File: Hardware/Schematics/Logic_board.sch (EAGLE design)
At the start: 42 parts, among them IC1 ADUM1250, J1 1X2-3.5MM, J2 3-PIN SMD, J3 3-PIN SMD, J4 3-PIN SMD, U1 ESP-32S

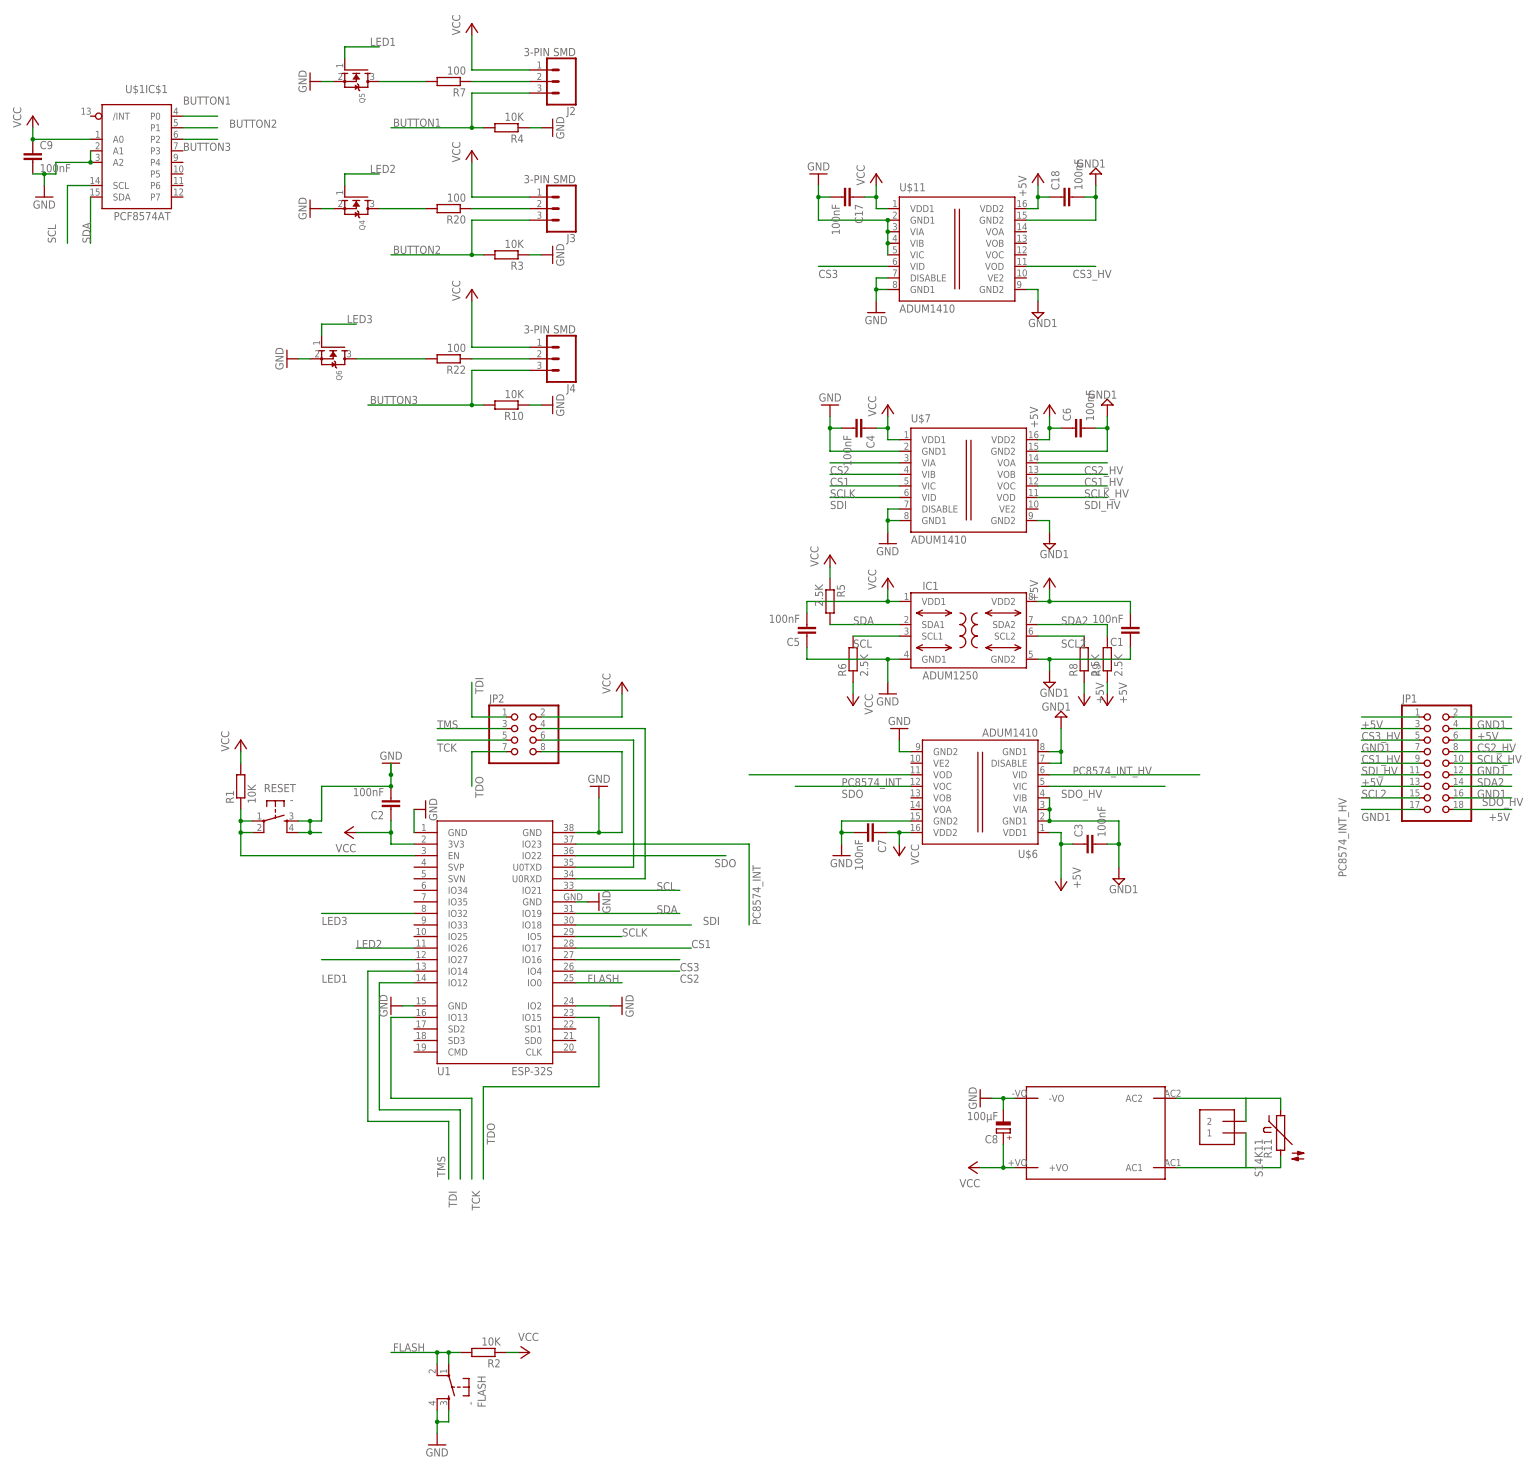
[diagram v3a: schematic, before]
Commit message: Work on changeing to FATFS. Not tested yet.
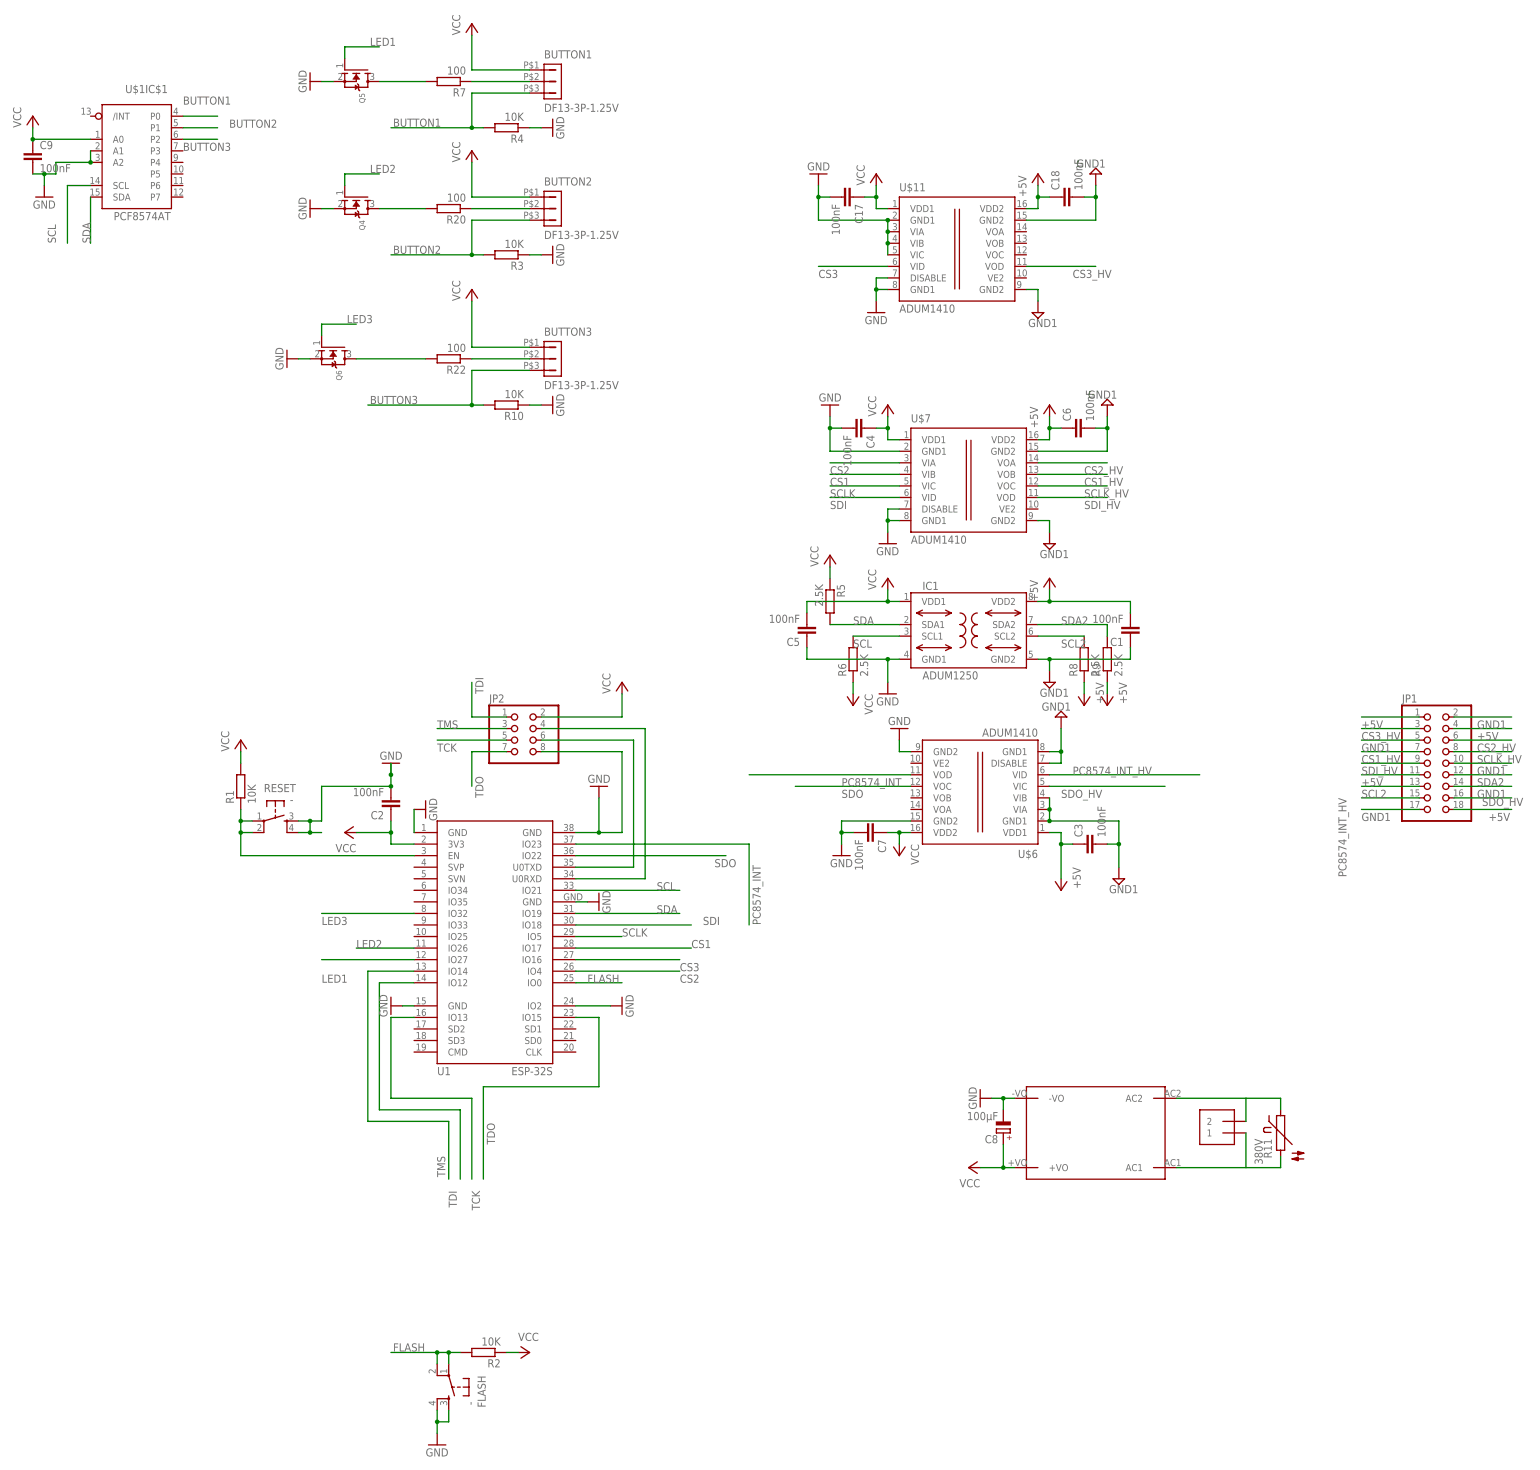
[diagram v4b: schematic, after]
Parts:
- removed J2, J3, J4: 3-PIN SMD, SparkFun-Connectors:CONN_03JST-SMD
- added BUTTON1, BUTTON2, BUTTON3: DF13-3P-1.25V, con-hirose-df13:DF13-3P-1.25V
- R11: value S14K11 -> 380V
- SUPPLY: value HLK-PM03 -> 5V
- renumbered U$8 to SUPPLY
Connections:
- net BUTTON1: now also BUTTON1.3; no longer J2.3
- net BUTTON2: now also BUTTON2.3; no longer J3.3
- net BUTTON3: now also BUTTON3.3; no longer J4.3
- net N$11: now also BUTTON3.2; no longer J4.2
- net N$7: now also BUTTON2.2; no longer J3.2
- net N$9: now also BUTTON1.2; no longer J2.2
- net VCC: now also BUTTON1.1, BUTTON2.1, BUTTON3.1; no longer J2.1, J3.1, J4.1
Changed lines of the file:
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@@
 <part name="GND15" library="supply1" deviceset="GND" device=""/>
 <part name="C4" library="rcl" library_urn="urn:adsk.eagle:library:334" deviceset="C-EU" device="C0805" value="100nF"/>
-<part name="U$8" library="PowerSocket" deviceset="HLK-PM03" device=""/>
+<part name="SUPPLY" library="PowerSocket" deviceset="HLK-PM03" device="" value="5V"/>
 <part name="J1" library="adafruit" deviceset="1X2" device="-3.5MM"/>
 <part name="GND16" library="supply1" deviceset="GND" device=""/>
@@
 <part name="GND21" library="supply1" deviceset="GND" device=""/>
 <part name="C9" library="rcl" library_urn="urn:adsk.eagle:library:334" deviceset="C-EU" device="C0805" value="100nF"/>
-<part name="R11" library="varistor" library_urn="urn:adsk.eagle:library:410" deviceset="S14K11" device=""/>
-<part name="J2" library="SparkFun-Connectors" deviceset="CONN_03" device="JST-SMD" value="3-PIN SMD"/>
-<part name="J3" library="SparkFun-Connectors" deviceset="CONN_03" device="JST-SMD" value="3-PIN SMD"/>
-<part name="J4" library="SparkFun-Connectors" deviceset="CONN_03" device="JST-SMD" value="3-PIN SMD"/>
+<part name="R11" library="varistor" library_urn="urn:adsk.eagle:library:410" deviceset="S14K11" device="" value="380V"/>
+<part name="BUTTON2" library="con-hirose-df13" deviceset="DF13-3P-1.25" device="V"/>
+<part name="BUTTON1" library="con-hirose-df13" deviceset="DF13-3P-1.25" device="V"/>
+<part name="BUTTON3" library="con-hirose-df13" deviceset="DF13-3P-1.25" device="V"/>
 </parts>
 <sheets>
@@
 <instance part="GND15" gate="1" x="99.06" y="91.44"/>
 <instance part="C4" gate="G$1" x="93.98" y="116.84" rot="R270"/>
-<instance part="U$8" gate="G$1" x="129.54" y="-38.1" rot="R180"/>
+<instance part="SUPPLY" gate="G$1" x="129.54" y="-38.1" rot="R180"/>
 <instance part="J1" gate="G$1" x="172.72" y="-35.56" rot="R180"/>
 <instance part="GND16" gate="1" x="119.38" y="-30.48" rot="R270"/>
@@
 <instance part="C9" gate="G$1" x="-88.9" y="177.8"/>
 <instance part="R11" gate="G$1" x="185.42" y="-38.1" rot="R270"/>
-<instance part="J2" gate="J$1" x="27.94" y="193.04" rot="R180"/>
-<instance part="J3" gate="J$1" x="27.94" y="165.1" rot="R180"/>
-<instance part="J4" gate="J$1" x="27.94" y="132.08" rot="R180"/>
+<instance part="BUTTON2" gate="G$1" x="25.4" y="165.1"/>
+<instance part="BUTTON1" gate="G$1" x="25.4" y="193.04"/>
+<instance part="BUTTON3" gate="G$1" x="25.4" y="132.08"/>
 </instances>
 <busses>
@@
 </segment>
 <segment>
-<pinref part="U$8" gate="G$1" pin="-VO"/>
+<pinref part="SUPPLY" gate="G$1" pin="-VO"/>
 <wire x1="127" y1="-30.48" x2="124.46" y2="-30.48" width="0.1524" layer="91"/>
 <pinref part="GND16" gate="1" pin="GND"/>
@@
 <wire x1="20.32" y1="195.58" x2="7.62" y2="195.58" width="0.1524" layer="91"/>
 <wire x1="7.62" y1="195.58" x2="7.62" y2="203.2" width="0.1524" layer="91"/>
-<pinref part="J2" gate="J$1" pin="1"/>
+<pinref part="BUTTON1" gate="G$1" pin="1"/>
 </segment>
 <segment>
@@
 <wire x1="20.32" y1="167.64" x2="7.62" y2="167.64" width="0.1524" layer="91"/>
 <wire x1="7.62" y1="167.64" x2="7.62" y2="175.26" width="0.1524" layer="91"/>
-<pinref part="J3" gate="J$1" pin="1"/>
+<pinref part="BUTTON2" gate="G$1" pin="1"/>
 </segment>
 <segment>
@@
 <wire x1="7.62" y1="144.78" x2="7.62" y2="134.62" width="0.1524" layer="91"/>
 <wire x1="20.32" y1="134.62" x2="7.62" y2="134.62" width="0.1524" layer="91"/>
-<pinref part="J4" gate="J$1" pin="1"/>
+<pinref part="BUTTON3" gate="G$1" pin="1"/>
 </segment>
 <segment>
@@
 </segment>
 <segment>
-<pinref part="U$8" gate="G$1" pin="+VO"/>
+<pinref part="SUPPLY" gate="G$1" pin="+VO"/>
 <wire x1="127" y1="-45.72" x2="124.46" y2="-45.72" width="0.1524" layer="91"/>
 <pinref part="P+11" gate="VCC" pin="VCC"/>
@@
 <wire x1="10.16" y1="182.88" x2="7.62" y2="182.88" width="0.1524" layer="91"/>
 <junction x="7.62" y="182.88"/>
-<pinref part="J2" gate="J$1" pin="3"/>
+<pinref part="BUTTON1" gate="G$1" pin="3"/>
 </segment>
 <segment>
@@
 <wire x1="10.16" y1="154.94" x2="7.62" y2="154.94" width="0.1524" layer="91"/>
 <junction x="7.62" y="154.94"/>
-<pinref part="J3" gate="J$1" pin="3"/>
+<pinref part="BUTTON2" gate="G$1" pin="3"/>
 </segment>
 <segment>
@@
 <wire x1="10.16" y1="121.92" x2="7.62" y2="121.92" width="0.1524" layer="91"/>
 <junction x="7.62" y="121.92"/>
-<pinref part="J4" gate="J$1" pin="3"/>
+<pinref part="BUTTON3" gate="G$1" pin="3"/>
 </segment>
 <segment>
@@
 <pinref part="R7" gate="G$1" pin="1"/>
 <wire x1="7.62" y1="193.04" x2="20.32" y2="193.04" width="0.1524" layer="91"/>
-<pinref part="J2" gate="J$1" pin="2"/>
+<pinref part="BUTTON1" gate="G$1" pin="2"/>
 </segment>
 </net>
@@
 <pinref part="R22" gate="G$1" pin="1"/>
 <wire x1="7.62" y1="132.08" x2="20.32" y2="132.08" width="0.1524" layer="91"/>
-<pinref part="J4" gate="J$1" pin="2"/>
+<pinref part="BUTTON3" gate="G$1" pin="2"/>
 </segment>
 </net>
@@
 <pinref part="R20" gate="G$1" pin="1"/>
 <wire x1="20.32" y1="165.1" x2="7.62" y2="165.1" width="0.1524" layer="91"/>
-<pinref part="J3" gate="J$1" pin="2"/>
+<pinref part="BUTTON2" gate="G$1" pin="2"/>
 </segment>
 </net>
@@
 <net name="AC2" class="0">
 <segment>
-<pinref part="U$8" gate="G$1" pin="AC2"/>
+<pinref part="SUPPLY" gate="G$1" pin="AC2"/>
 <pinref part="J1" gate="G$1" pin="2"/>
 <wire x1="162.56" y1="-30.48" x2="177.8" y2="-30.48" width="0.1524" layer="91"/>
@@
 <pinref part="J1" gate="G$1" pin="1"/>
 <wire x1="177.8" y1="-38.1" x2="177.8" y2="-45.72" width="0.1524" layer="91"/>
-<pinref part="U$8" gate="G$1" pin="AC1"/>
+<pinref part="SUPPLY" gate="G$1" pin="AC1"/>
 <wire x1="177.8" y1="-45.72" x2="162.56" y2="-45.72" width="0.1524" layer="91"/>
 <pinref part="R11" gate="G$1" pin="2"/>

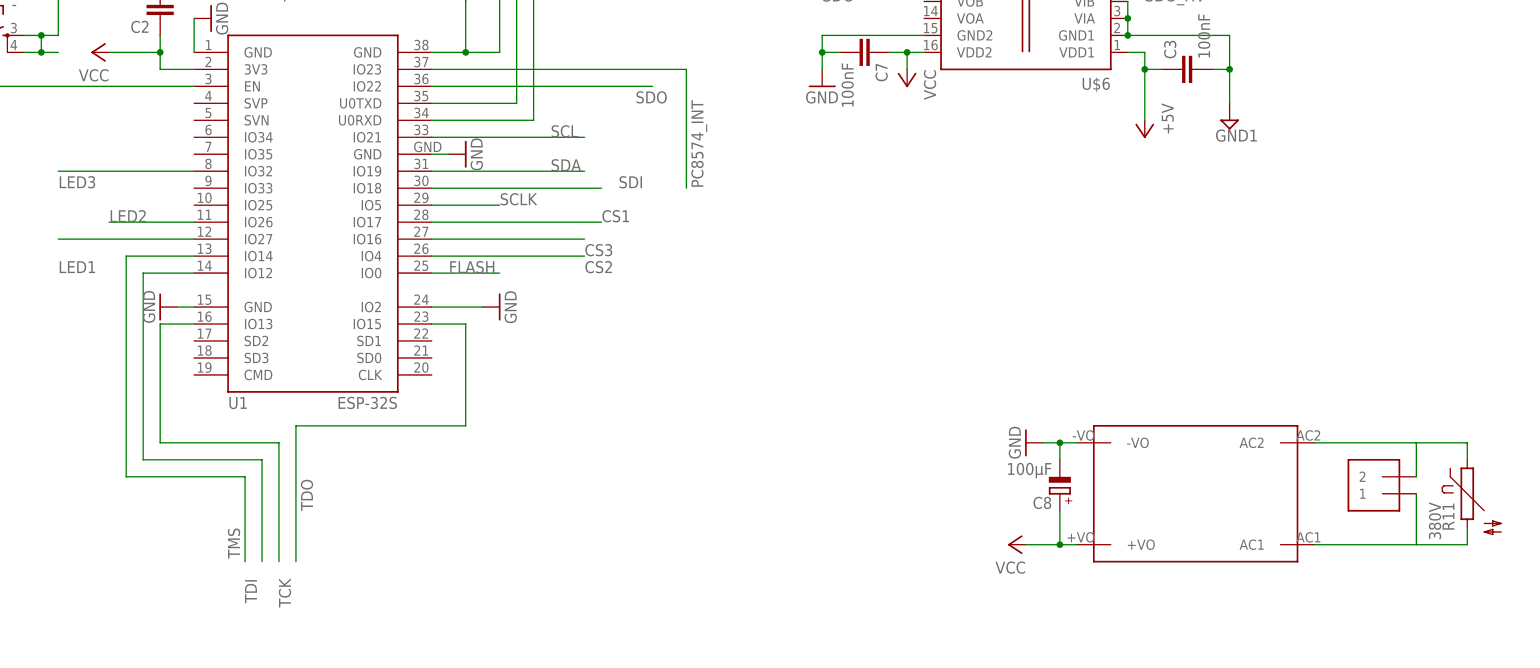
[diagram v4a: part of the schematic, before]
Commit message: Migrated filesystem to FAT32.
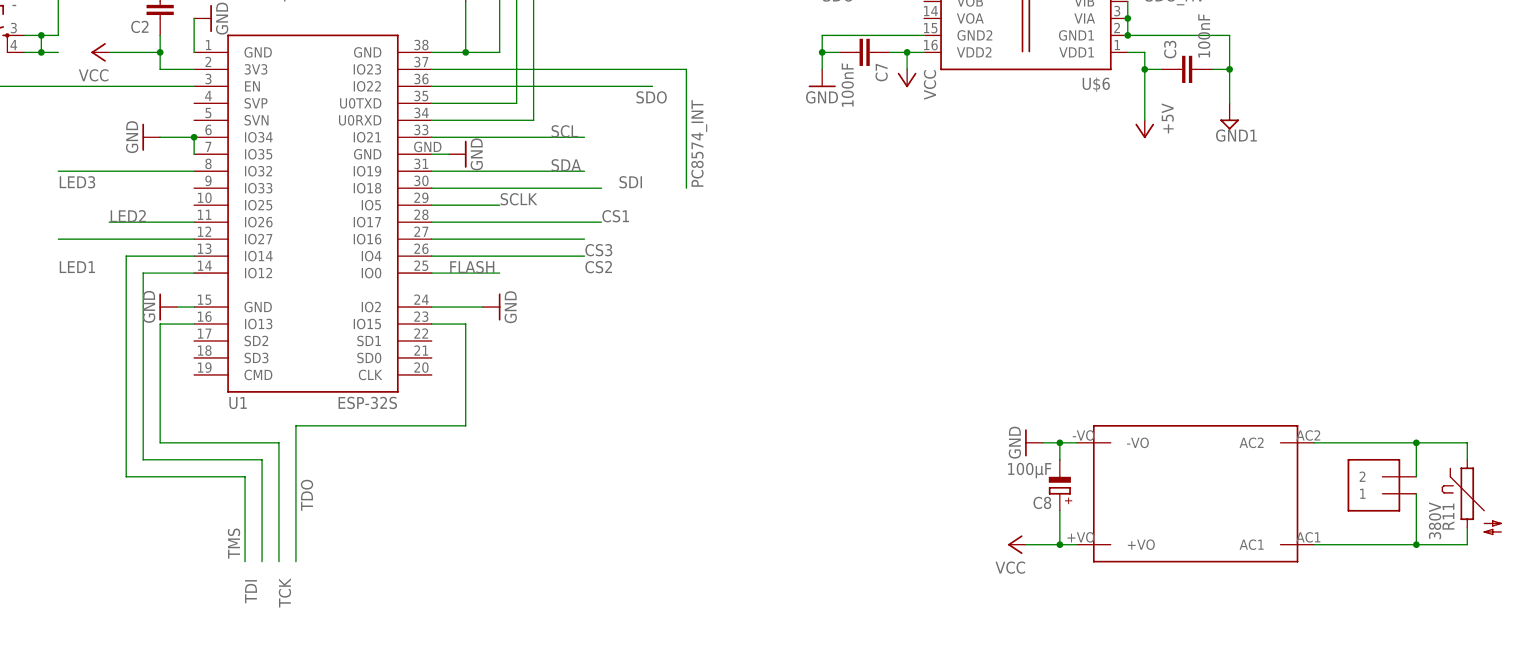
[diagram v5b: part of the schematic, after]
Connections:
- net GND: now also U1.IO34, U1.IO35
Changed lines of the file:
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@@
 <part name="BUTTON1" library="con-hirose-df13" deviceset="DF13-3P-1.25" device="V"/>
 <part name="BUTTON3" library="con-hirose-df13" deviceset="DF13-3P-1.25" device="V"/>
+<part name="GND22" library="supply1" deviceset="GND" device=""/>
 </parts>
 <sheets>
@@
 <instance part="BUTTON1" gate="G$1" x="25.4" y="193.04"/>
 <instance part="BUTTON3" gate="G$1" x="25.4" y="132.08"/>
+<instance part="GND22" gate="1" x="-12.7" y="15.24" rot="R270"/>
 </instances>
 <busses>
@@
 <wire x1="20.32" y1="121.92" x2="22.86" y2="121.92" width="0.1524" layer="91"/>
 </segment>
+<segment>
+<pinref part="GND22" gate="1" pin="GND"/>
+<pinref part="U1" gate="G$1" pin="IO34"/>
+<wire x1="-10.16" y1="15.24" x2="-5.08" y2="15.24" width="0.1524" layer="91"/>
+<pinref part="U1" gate="G$1" pin="IO35"/>
+<wire x1="-5.08" y1="15.24" x2="-5.08" y2="12.7" width="0.1524" layer="91"/>
+<junction x="-5.08" y="15.24"/>
+</segment>
 </net>
 <net name="VCC" class="0">
@@
 <wire x1="185.42" y1="-33.02" x2="185.42" y2="-30.48" width="0.1524" layer="91"/>
 <wire x1="185.42" y1="-30.48" x2="177.8" y2="-30.48" width="0.1524" layer="91"/>
+<junction x="177.8" y="-30.48"/>
 </segment>
 </net>
@@
 <wire x1="185.42" y1="-43.18" x2="185.42" y2="-45.72" width="0.1524" layer="91"/>
 <wire x1="185.42" y1="-45.72" x2="177.8" y2="-45.72" width="0.1524" layer="91"/>
-</segment>
-</net>
+<junction x="177.8" y="-45.72"/>
+</segment>
+</net>

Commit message: Updated board versions to final (v1) version, and added renders.
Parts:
- JP1: device pinhead:PINHD-2X9/90 -> pinhead:PINHD-2X9
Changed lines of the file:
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@@
 <part name="GND3" library="supply1" deviceset="GND" device=""/>
 <part name="P+7" library="supply1" deviceset="VCC" device=""/>
-<part name="JP1" library="pinhead" library_urn="urn:adsk.eagle:library:325" deviceset="PINHD-2X9" device="/90"/>
+<part name="JP1" library="pinhead" library_urn="urn:adsk.eagle:library:325" deviceset="PINHD-2X9" device=""/>
 <part name="R8" library="rcl" deviceset="R-EU_" device="R0805" value="2.5K"/>
 <part name="R9" library="rcl" deviceset="R-EU_" device="R0805" value="2.5K"/>
